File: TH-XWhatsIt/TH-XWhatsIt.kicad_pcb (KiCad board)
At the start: 2 copper layers, 145.3 x 129.6 mm, 32 parts, among them J1 MODEL F, J2 EXPANSION, J3 EXPANSION HEADER, J4 EXPANSION BEAMSPRING, J5 BEAMSPRING CONNECTOR, J6 EXPANSION BEAMSPRING, J7 EXPANSION DISPLAYWRITER, J8 DISPLAYWRITER CONNECTOR, J9 EXPANSION DISPLAYWRITER, U1 MCP4921-EP, U2 LM339, U3 74HCT595, U4 74HCT595, U5 ProMicro, U6 LM339, U7 74HCT595

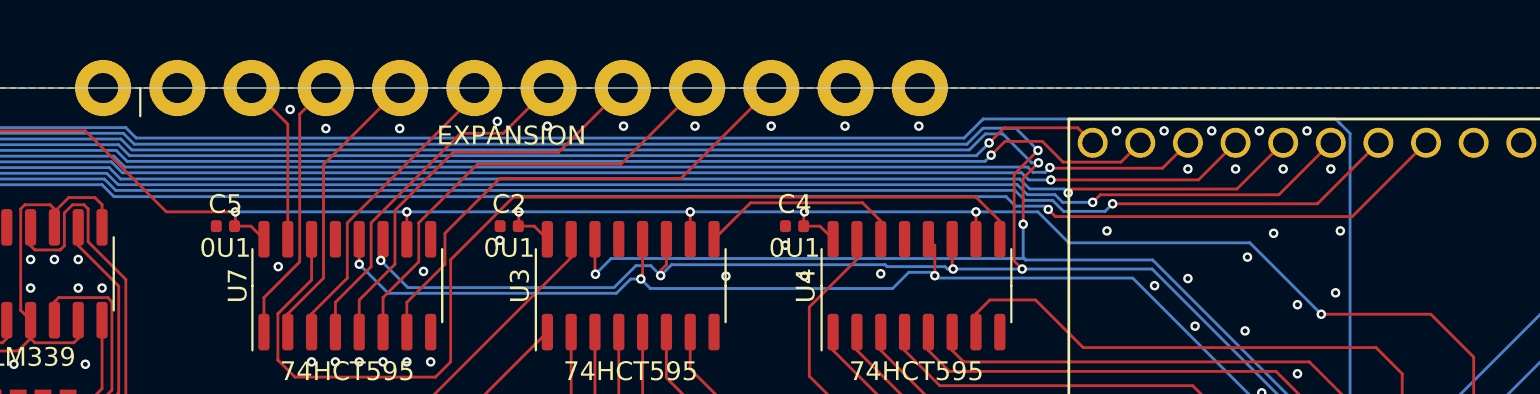
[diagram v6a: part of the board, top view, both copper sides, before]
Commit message: Reordered row to promicro pin connections to make sure that beamsprings only use two different ports
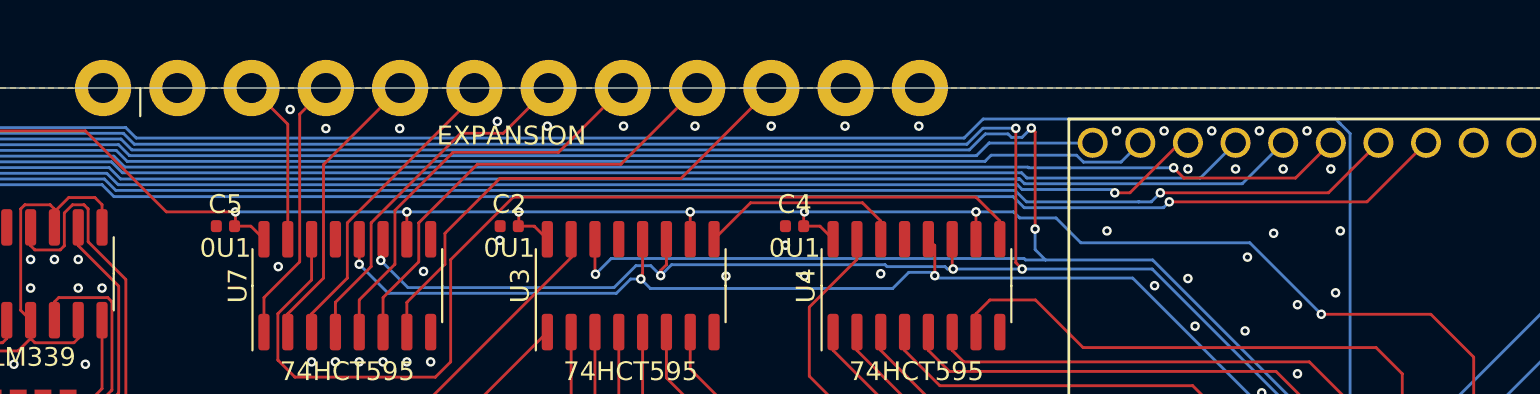
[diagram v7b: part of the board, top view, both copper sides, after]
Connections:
- U5 pad 10: ROW2 -> ROW6
- U5 pad 7: ROW6 -> ROW2
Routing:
- net ROW6: track 80.2 -> 72.2 mm
- net ROW2: track 90.7 -> 98.6 mm
- net CLOCK: track 178.0 -> 177.0 mm
- net MOSI: track 168.3 -> 169.4 mm
- net ROW1: track 88.6 -> 87.9 mm, vias 2 -> 1
- net ROW3: track 86.9 -> 86.3 mm, vias 2 -> 1
- net ROW5: track 80.5 -> 80.2 mm, vias 2 -> 1
- net ROW4: track 90.7 -> 90.6 mm, vias 2 -> 1

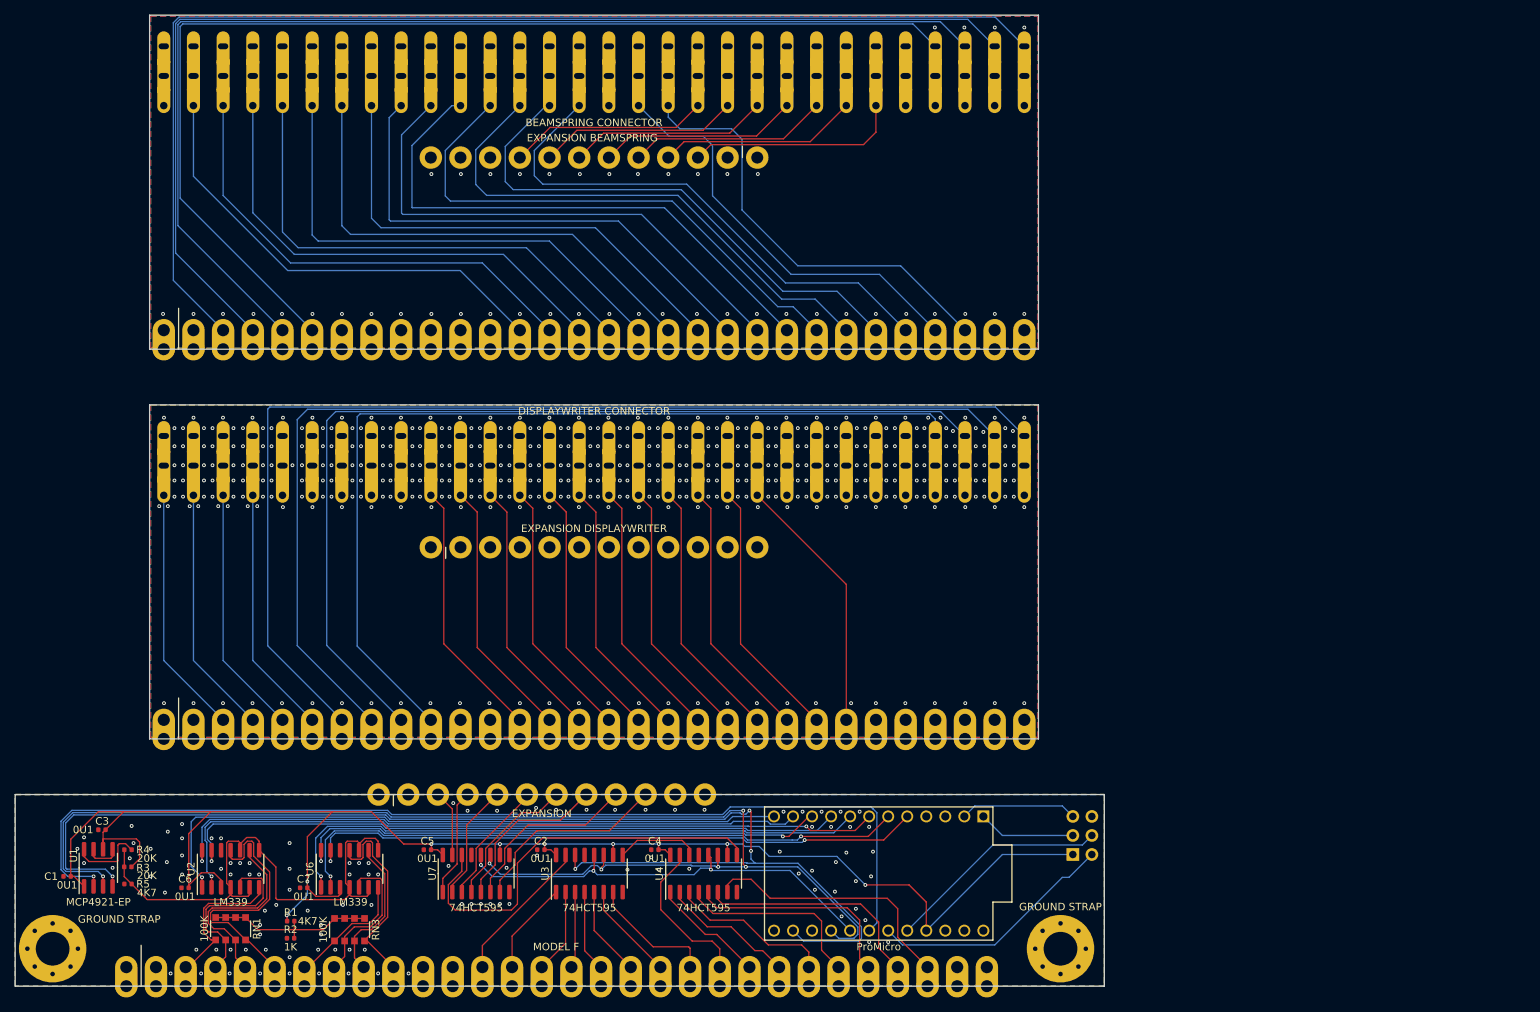
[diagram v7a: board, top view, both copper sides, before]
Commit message: pcb: move plugboards to the left, to demonstrate misalignment
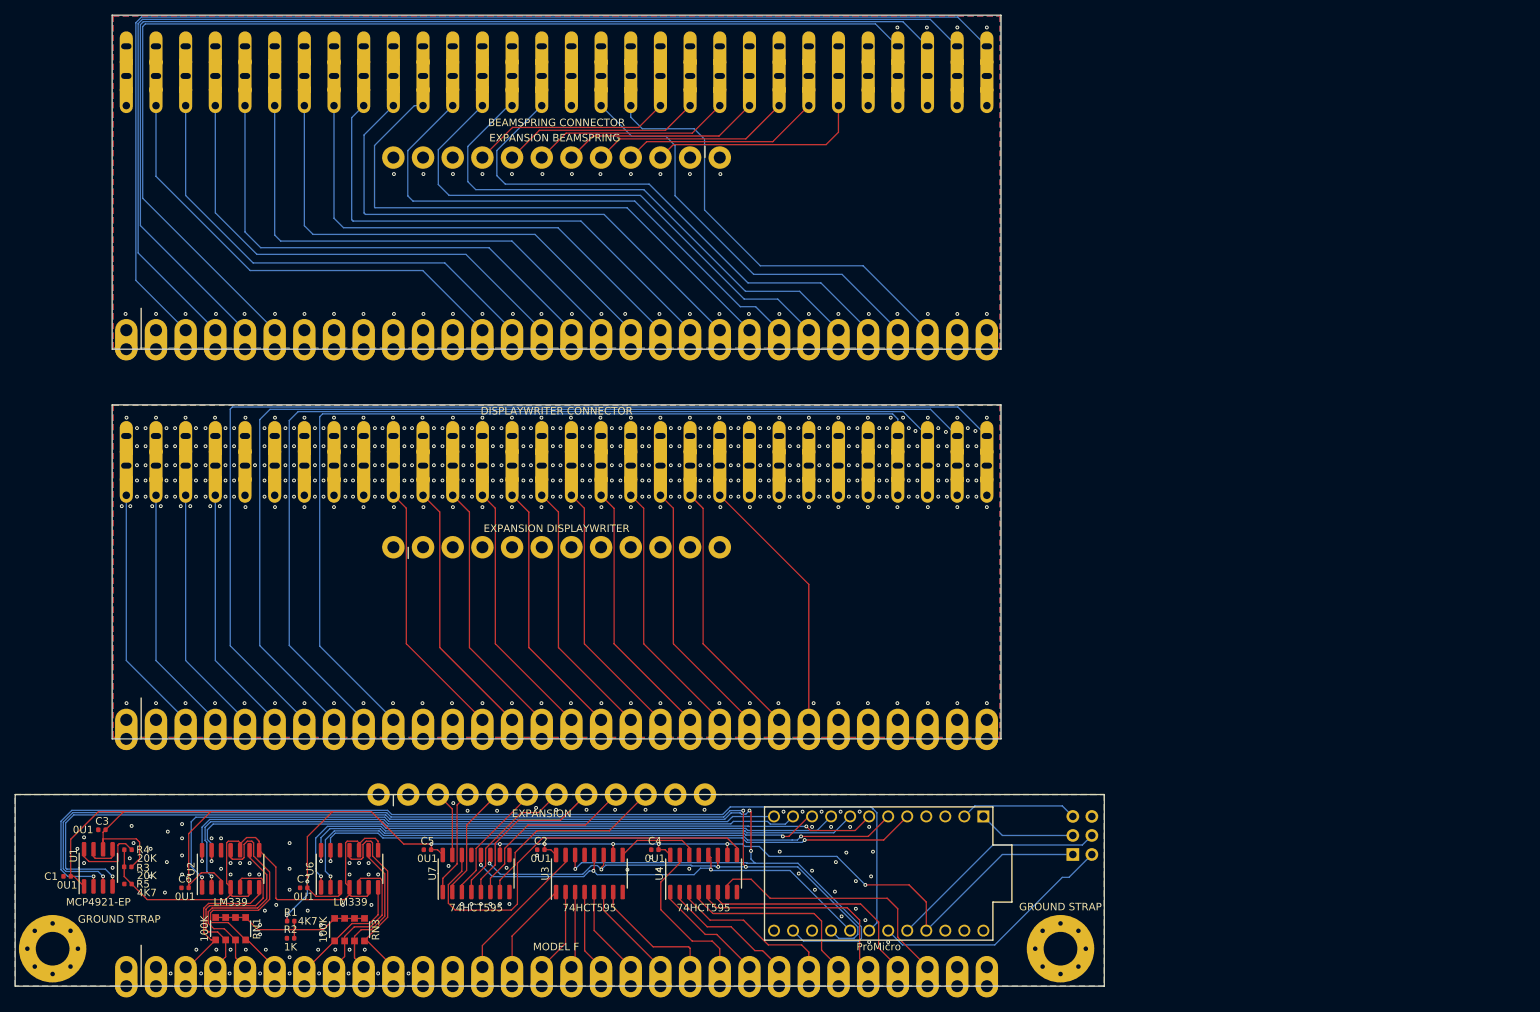
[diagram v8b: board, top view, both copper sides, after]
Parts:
- moved J4 5.00 mm to (102.9, 69.0)
- moved J5 5.00 mm to (102.9, 34.5)
- moved J6 5.00 mm to (102.9, 43.4)
- moved J7 5.00 mm to (102.9, 121.0)
- moved J8 5.00 mm to (102.9, 86.5)
- moved J9 5.00 mm to (102.9, 95.4)
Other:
- outline, holes or cut-outs redrawn
